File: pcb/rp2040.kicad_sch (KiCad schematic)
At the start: 20 parts, among them SW401 SW_Push, U401 RP2040, Y401 ABM8-272-T3

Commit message: add footprints
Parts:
- C401, C402, C403, C404, C405, C406, C407, C408, C409, C410, C411, C412, C413, C414: footprint (none) -> Capacitor_SMD:C_1210_3225Metric_Pad1.33x2.70mm_HandSolder
- R401, R402, R403: footprint (none) -> Resistor_SMD:R_1210_3225Metric_Pad1.30x2.65mm_HandSolder
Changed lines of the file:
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@@
 			)
 		)
-		(property "Footprint" ""
+		(property "Footprint" "Capacitor_SMD:C_1210_3225Metric_Pad1.33x2.70mm_HandSolder"
 			(at 225.7552 45.72 0)
 			(effects
@@
 			)
 		)
-		(property "Footprint" ""
+		(property "Footprint" "Capacitor_SMD:C_1210_3225Metric_Pad1.33x2.70mm_HandSolder"
 			(at 46.99 123.4948 0)
 			(effects
@@
 			)
 		)
-		(property "Footprint" ""
+		(property "Footprint" "Resistor_SMD:R_1210_3225Metric_Pad1.30x2.65mm_HandSolder"
 			(at 99.06 90.678 90)
 			(effects
@@
 			)
 		)
-		(property "Footprint" ""
+		(property "Footprint" "Resistor_SMD:R_1210_3225Metric_Pad1.30x2.65mm_HandSolder"
 			(at 46.482 55.88 90)
 			(effects
@@
 			)
 		)
-		(property "Footprint" ""
+		(property "Footprint" "Capacitor_SMD:C_1210_3225Metric_Pad1.33x2.70mm_HandSolder"
 			(at 191.4652 45.72 0)
 			(effects
@@
 			)
 		)
-		(property "Footprint" ""
+		(property "Footprint" "Capacitor_SMD:C_1210_3225Metric_Pad1.33x2.70mm_HandSolder"
 			(at 237.1852 45.72 0)
 			(effects
@@
 			)
 		)
-		(property "Footprint" ""
+		(property "Footprint" "Resistor_SMD:R_1210_3225Metric_Pad1.30x2.65mm_HandSolder"
 			(at 99.06 88.138 90)
 			(effects
@@
 			)
 		)
-		(property "Footprint" ""
+		(property "Footprint" "Capacitor_SMD:C_1210_3225Metric_Pad1.33x2.70mm_HandSolder"
 			(at 168.6052 60.96 0)
 			(effects
@@
 			)
 		)
-		(property "Footprint" ""
+		(property "Footprint" "Capacitor_SMD:C_1210_3225Metric_Pad1.33x2.70mm_HandSolder"
 			(at 214.3252 45.72 0)
 			(effects
@@
 			)
 		)
-		(property "Footprint" ""
+		(property "Footprint" "Capacitor_SMD:C_1210_3225Metric_Pad1.33x2.70mm_HandSolder"
 			(at 127.9652 45.72 0)
 			(effects
@@
 			)
 		)
-		(property "Footprint" ""
+		(property "Footprint" "Capacitor_SMD:C_1210_3225Metric_Pad1.33x2.70mm_HandSolder"
 			(at 180.0352 45.72 0)
 			(effects
@@
 			)
 		)
-		(property "Footprint" ""
+		(property "Footprint" "Capacitor_SMD:C_1210_3225Metric_Pad1.33x2.70mm_HandSolder"
 			(at 202.8952 45.72 0)
 			(effects
@@
 			)
 		)
-		(property "Footprint" ""
+		(property "Footprint" "Capacitor_SMD:C_1210_3225Metric_Pad1.33x2.70mm_HandSolder"
 			(at 168.6052 45.72 0)
 			(effects
@@
 			)
 		)
-		(property "Footprint" ""
+		(property "Footprint" "Capacitor_SMD:C_1210_3225Metric_Pad1.33x2.70mm_HandSolder"
 			(at 46.99 133.6548 0)
 			(effects
@@
 			)
 		)
-		(property "Footprint" ""
+		(property "Footprint" "Capacitor_SMD:C_1210_3225Metric_Pad1.33x2.70mm_HandSolder"
 			(at 36.83 49.8348 0)
 			(effects
@@
 			)
 		)
-		(property "Footprint" ""
+		(property "Footprint" "Capacitor_SMD:C_1210_3225Metric_Pad1.33x2.70mm_HandSolder"
 			(at 133.0452 60.96 0)
 			(effects
@@
 			)
 		)
-		(property "Footprint" ""
+		(property "Footprint" "Capacitor_SMD:C_1210_3225Metric_Pad1.33x2.70mm_HandSolder"
 			(at 116.5352 45.72 0)
 			(effects

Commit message: add footprints
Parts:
- SW401: footprint (none) -> rp2040-devboard:SW_SPST_EVPBV; Distributor link (none) -> https://mou.sr/4aZdR1f
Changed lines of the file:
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@@
 			)
 		)
-		(property "Footprint" ""
+		(property "Footprint" "rp2040-devboard:SW_SPST_EVPBV"
 			(at 33.02 57.15 0)
 			(effects
@@
 			(at 33.02 62.23 0)
 			(effects
+				(font
+					(size 1.27 1.27)
+				)
+				(hide yes)
+			)
+		)
+		(property "Distributor link" "https://mou.sr/4aZdR1f"
+			(at 33.02 62.23 0)
+			(effects

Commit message: add footprints + expose grounds and power on pins
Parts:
- Y401: footprint (none) -> Crystal:Crystal_SMD_3225-4Pin_3.2x2.5mm
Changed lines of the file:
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@@
 			)
 		)
-		(property "Footprint" ""
+		(property "Footprint" "Crystal:Crystal_SMD_3225-4Pin_3.2x2.5mm"
 			(at 60.96 129.54 0)
 			(effects

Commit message: wip pcb placement
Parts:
- removed R401: TBD, Resistor_SMD:R_1210_3225Metric_Pad1.30x2.65mm_HandSolder, symbol Device:R
- renumbered R402 to R401, R403 to R402
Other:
- note added: "There is already an on-chip pull-up resistor of 50k-80k"
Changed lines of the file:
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@@
-	)
-	(junction
-		(at 48.26 62.23)
-		(diameter 0)
-		(color 0 0 0 0)
 	)
 	(junction
@@
 	(wire
 		(pts
-			(xy 48.26 59.69) (xy 48.26 62.23)
-		)
-		(stroke
-			(width 0)
-			(type default)
-		)
-	)
-	(wire
-		(pts
 			(xy 175.26 124.46) (xy 171.45 124.46)
 		)
@@
 	(wire
 		(pts
-			(xy 44.45 62.23) (xy 48.26 62.23)
-		)
-		(stroke
-			(width 0)
-			(type default)
-		)
-	)
-	(wire
-		(pts
 			(xy 39.37 124.46) (xy 34.29 124.46)
 		)
@@
 	(wire
 		(pts
-			(xy 48.26 62.23) (xy 59.69 62.23)
+			(xy 44.45 62.23) (xy 59.69 62.23)
 		)
 		(stroke
@@
 		(pts
 			(xy 116.84 134.62) (xy 120.65 134.62)
-		)
-		(stroke
-			(width 0)
-			(type default)
-		)
-	)
-	(wire
-		(pts
-			(xy 48.26 49.53) (xy 48.26 52.07)
 		)
 		(stroke
@@
 		(exclude_from_sim no)
 		(at 37.846 37.846 0)
+		(effects
+			(font
+				(size 1.27 1.27)
+			)
+		)
+	)
+	(text "There is already an on-chip pull-up resistor of 50k-80k"
+		(exclude_from_sim no)
+		(at 44.958 72.39 0)
 		(effects
 			(font
@@
 		(on_board yes)
 		(dnp no)
-		(property "Reference" "R403"
+		(property "Reference" "R402"
 			(at 99.06 91.44 90)
 			(effects
@@
 			(project "rp2040-devboard"
 				(path "/b920ba62-ae29-4be1-8493-2f85fc152395/f6b75d06-e2a8-4cde-87f9-edbb0b8d1ddb"
-					(reference "R403")
+					(reference "R402")
 					(unit 1)
 				)
@@
 	)
 	(symbol
-		(lib_id "Device:R")
-		(at 48.26 55.88 0)
-		(unit 1)
-		(exclude_from_sim no)
-		(in_bom yes)
-		(on_board yes)
-		(dnp no)
-		(fields_autoplaced yes)
-		(property "Reference" "R401"
-			(at 50.8 54.6099 0)
-			(effects
-				(font
-					(size 1.27 1.27)
-				)
-				(justify left)
-			)
-		)
-		(property "Value" "TBD"
-			(at 50.8 57.1499 0)
-			(effects
-				(font
-					(size 1.27 1.27)
-				)
-				(justify left)
-			)
-		)
-		(property "Footprint" "Resistor_SMD:R_1210_3225Metric_Pad1.30x2.65mm_HandSolder"
-			(at 46.482 55.88 90)
-			(effects
-				(font
-					(size 1.27 1.27)
-				)
-				(hide yes)
-			)
-		)
-		(property "Datasheet" "~"
-			(at 48.26 55.88 0)
-			(effects
-				(font
-					(size 1.27 1.27)
-				)
-				(hide yes)
-			)
-		)
-		(property "Description" "Resistor"
-			(at 48.26 55.88 0)
-			(effects
-				(font
-					(size 1.27 1.27)
-				)
-				(hide yes)
-			)
-		)
-		(pin "1"
-		)
-		(pin "2"
-		)
-		(instances
-			(project "rp2040-devboard"
-				(path "/b920ba62-ae29-4be1-8493-2f85fc152395/f6b75d06-e2a8-4cde-87f9-edbb0b8d1ddb"
-					(reference "R401")
-					(unit 1)
-				)
-			)
-		)
-	)
-	(symbol
 		(lib_id "Device:C")
 		(at 190.5 41.91 0)
@@
 				(path "/b920ba62-ae29-4be1-8493-2f85fc152395/f6b75d06-e2a8-4cde-87f9-edbb0b8d1ddb"
 					(reference "C407")
-					(unit 1)
-				)
-			)
-		)
-	)
-	(symbol
-		(lib_id "power:+3V3")
-		(at 48.26 49.53 0)
-		(unit 1)
-		(exclude_from_sim no)
-		(in_bom yes)
-		(on_board yes)
-		(dnp no)
-		(fields_autoplaced yes)
-		(property "Reference" "#PWR05"
-			(at 48.26 53.34 0)
-			(effects
-				(font
-					(size 1.27 1.27)
-				)
-				(hide yes)
-			)
-		)
-		(property "Value" "+3V3"
-			(at 48.26 44.45 0)
-			(effects
-				(font
-					(size 1.27 1.27)
-				)
-			)
-		)
-		(property "Footprint" ""
-			(at 48.26 49.53 0)
-			(effects
-				(font
-					(size 1.27 1.27)
-				)
-				(hide yes)
-			)
-		)
-		(property "Datasheet" ""
-			(at 48.26 49.53 0)
-			(effects
-				(font
-					(size 1.27 1.27)
-				)
-				(hide yes)
-			)
-		)
-		(property "Description" "Power symbol creates a global label with name \"+3V3\""
-			(at 48.26 49.53 0)
-			(effects
-				(font
-					(size 1.27 1.27)
-				)
-				(hide yes)
-			)
-		)
-		(pin "1"
-		)
-		(instances
-			(project "rp2040-devboard"
-				(path "/b920ba62-ae29-4be1-8493-2f85fc152395/f6b75d06-e2a8-4cde-87f9-edbb0b8d1ddb"
-					(reference "#PWR05")
 					(unit 1)
 				)
@@
 		(on_board yes)
 		(dnp no)
-		(property "Reference" "R402"
+		(property "Reference" "R401"
 			(at 99.06 81.28 90)
 			(effects
@@
 			(project "rp2040-devboard"
 				(path "/b920ba62-ae29-4be1-8493-2f85fc152395/f6b75d06-e2a8-4cde-87f9-edbb0b8d1ddb"
-					(reference "R402")
+					(reference "R401")
 					(unit 1)
 				)

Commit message: change footprint
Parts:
- C401, C402, C403, C404, C405, C406, C407, C408, C409, C410, C411, C412, C413, C414: footprint Capacitor_SMD:C_1210_3225Metric_Pad1.33x2.70mm_HandSolder -> Capacitor_SMD:C_0603_1608Metric_Pad1.08x0.95mm_HandSolder
- R401, R402: footprint Resistor_SMD:R_1210_3225Metric_Pad1.30x2.65mm_HandSolder -> Resistor_SMD:R_0603_1608Metric_Pad0.98x0.95mm_HandSolder
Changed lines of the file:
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@@
 			)
 		)
-		(property "Footprint" "Capacitor_SMD:C_1210_3225Metric_Pad1.33x2.70mm_HandSolder"
+		(property "Footprint" "Capacitor_SMD:C_0603_1608Metric_Pad1.08x0.95mm_HandSolder"
 			(at 225.7552 45.72 0)
 			(effects
@@
 			)
 		)
-		(property "Footprint" "Capacitor_SMD:C_1210_3225Metric_Pad1.33x2.70mm_HandSolder"
+		(property "Footprint" "Capacitor_SMD:C_0603_1608Metric_Pad1.08x0.95mm_HandSolder"
 			(at 46.99 123.4948 0)
 			(effects
@@
 			)
 		)
-		(property "Footprint" "Resistor_SMD:R_1210_3225Metric_Pad1.30x2.65mm_HandSolder"
+		(property "Footprint" "Resistor_SMD:R_0603_1608Metric_Pad0.98x0.95mm_HandSolder"
 			(at 99.06 90.678 90)
 			(effects
@@
 			)
 		)
-		(property "Footprint" "Capacitor_SMD:C_1210_3225Metric_Pad1.33x2.70mm_HandSolder"
+		(property "Footprint" "Capacitor_SMD:C_0603_1608Metric_Pad1.08x0.95mm_HandSolder"
 			(at 191.4652 45.72 0)
 			(effects
@@
 			)
 		)
-		(property "Footprint" "Capacitor_SMD:C_1210_3225Metric_Pad1.33x2.70mm_HandSolder"
+		(property "Footprint" "Capacitor_SMD:C_0603_1608Metric_Pad1.08x0.95mm_HandSolder"
 			(at 237.1852 45.72 0)
 			(effects
@@
 			)
 		)
-		(property "Footprint" "Resistor_SMD:R_1210_3225Metric_Pad1.30x2.65mm_HandSolder"
+		(property "Footprint" "Resistor_SMD:R_0603_1608Metric_Pad0.98x0.95mm_HandSolder"
 			(at 99.06 88.138 90)
 			(effects
@@
 			)
 		)
-		(property "Footprint" "Capacitor_SMD:C_1210_3225Metric_Pad1.33x2.70mm_HandSolder"
+		(property "Footprint" "Capacitor_SMD:C_0603_1608Metric_Pad1.08x0.95mm_HandSolder"
 			(at 168.6052 60.96 0)
 			(effects
@@
 			)
 		)
-		(property "Footprint" "Capacitor_SMD:C_1210_3225Metric_Pad1.33x2.70mm_HandSolder"
+		(property "Footprint" "Capacitor_SMD:C_0603_1608Metric_Pad1.08x0.95mm_HandSolder"
 			(at 214.3252 45.72 0)
 			(effects
@@
 			)
 		)
-		(property "Footprint" "Capacitor_SMD:C_1210_3225Metric_Pad1.33x2.70mm_HandSolder"
+		(property "Footprint" "Capacitor_SMD:C_0603_1608Metric_Pad1.08x0.95mm_HandSolder"
 			(at 127.9652 45.72 0)
 			(effects
@@
 			)
 		)
-		(property "Footprint" "Capacitor_SMD:C_1210_3225Metric_Pad1.33x2.70mm_HandSolder"
+		(property "Footprint" "Capacitor_SMD:C_0603_1608Metric_Pad1.08x0.95mm_HandSolder"
 			(at 180.0352 45.72 0)
 			(effects
@@
 			)
 		)
-		(property "Footprint" "Capacitor_SMD:C_1210_3225Metric_Pad1.33x2.70mm_HandSolder"
+		(property "Footprint" "Capacitor_SMD:C_0603_1608Metric_Pad1.08x0.95mm_HandSolder"
 			(at 202.8952 45.72 0)
 			(effects
@@
 			)
 		)
-		(property "Footprint" "Capacitor_SMD:C_1210_3225Metric_Pad1.33x2.70mm_HandSolder"
+		(property "Footprint" "Capacitor_SMD:C_0603_1608Metric_Pad1.08x0.95mm_HandSolder"
 			(at 168.6052 45.72 0)
 			(effects
@@
 			)
 		)
-		(property "Footprint" "Capacitor_SMD:C_1210_3225Metric_Pad1.33x2.70mm_HandSolder"
+		(property "Footprint" "Capacitor_SMD:C_0603_1608Metric_Pad1.08x0.95mm_HandSolder"
 			(at 46.99 133.6548 0)
 			(effects
@@
 			)
 		)
-		(property "Footprint" "Capacitor_SMD:C_1210_3225Metric_Pad1.33x2.70mm_HandSolder"
+		(property "Footprint" "Capacitor_SMD:C_0603_1608Metric_Pad1.08x0.95mm_HandSolder"
 			(at 36.83 49.8348 0)
 			(effects
@@
 			)
 		)
-		(property "Footprint" "Capacitor_SMD:C_1210_3225Metric_Pad1.33x2.70mm_HandSolder"
+		(property "Footprint" "Capacitor_SMD:C_0603_1608Metric_Pad1.08x0.95mm_HandSolder"
 			(at 133.0452 60.96 0)
 			(effects
@@
 			)
 		)
-		(property "Footprint" "Capacitor_SMD:C_1210_3225Metric_Pad1.33x2.70mm_HandSolder"
+		(property "Footprint" "Capacitor_SMD:C_0603_1608Metric_Pad1.08x0.95mm_HandSolder"
 			(at 116.5352 45.72 0)
 			(effects

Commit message: finish routing
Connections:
- net USB_D+: now also R401.1; no longer R402.1
- net USB_D-: now also R402.1; no longer R401.1
- net USB_TERM_D-: now reaches R402.2, U401.46 (USB_DM)
- net USB_TERM_D+: now reaches R401.2, U401.47 (USB_DP)

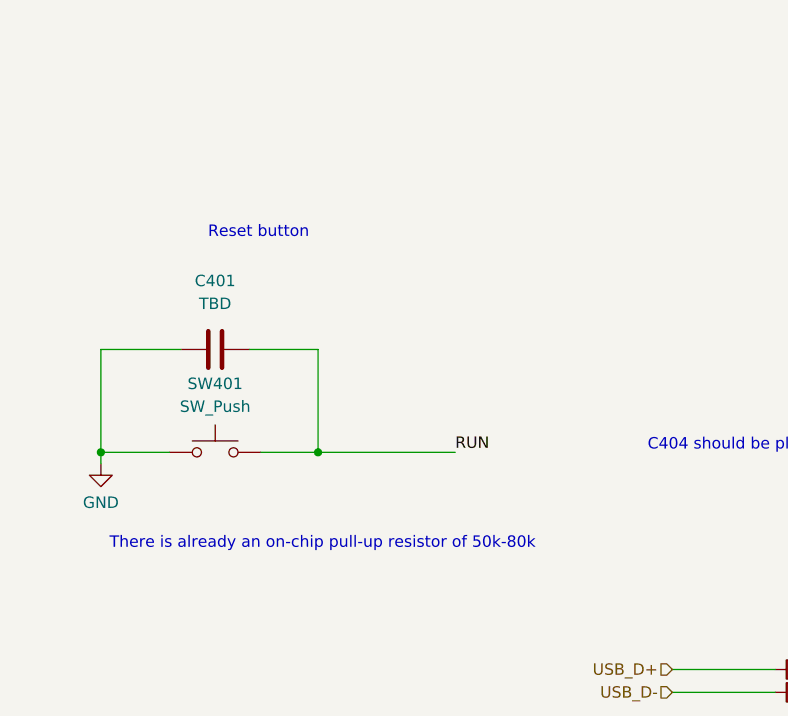
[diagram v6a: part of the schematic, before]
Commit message: add debouncing capacitor value and dnp pull up
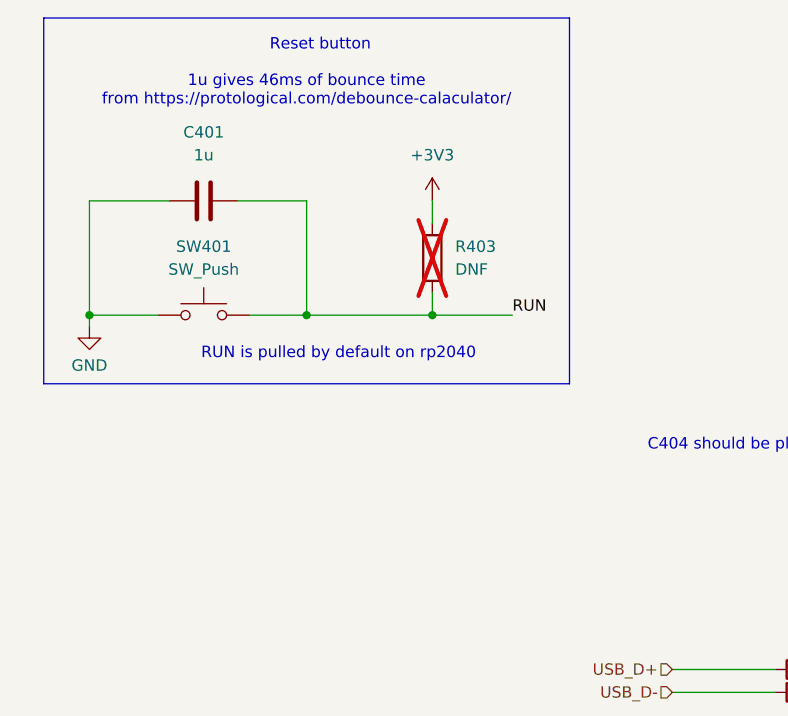
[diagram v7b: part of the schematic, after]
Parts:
- added R403: DNF, Resistor_SMD:R_0603_1608Metric_Pad0.98x0.95mm_HandSolder, symbol Device:R
- C401: value TBD -> 1u
- U401: Distributor link (none) -> https://mou.sr/3yOwNm4
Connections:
- net +3V3: now also R403.1
- net RUN: now also R403.2
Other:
- note added: "1u gives 46ms of bounce time from https://protological.com/debounce-calaculator/"
- note added: "RUN is pulled by default on rp2040"
- note removed: "There is already an on-chip pull-up resistor of 50k-80k"
- moved on the sheet: C401, SW401
